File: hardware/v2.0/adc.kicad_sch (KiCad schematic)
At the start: 1 part, among them U1 ECP5U-25F-CABGA256

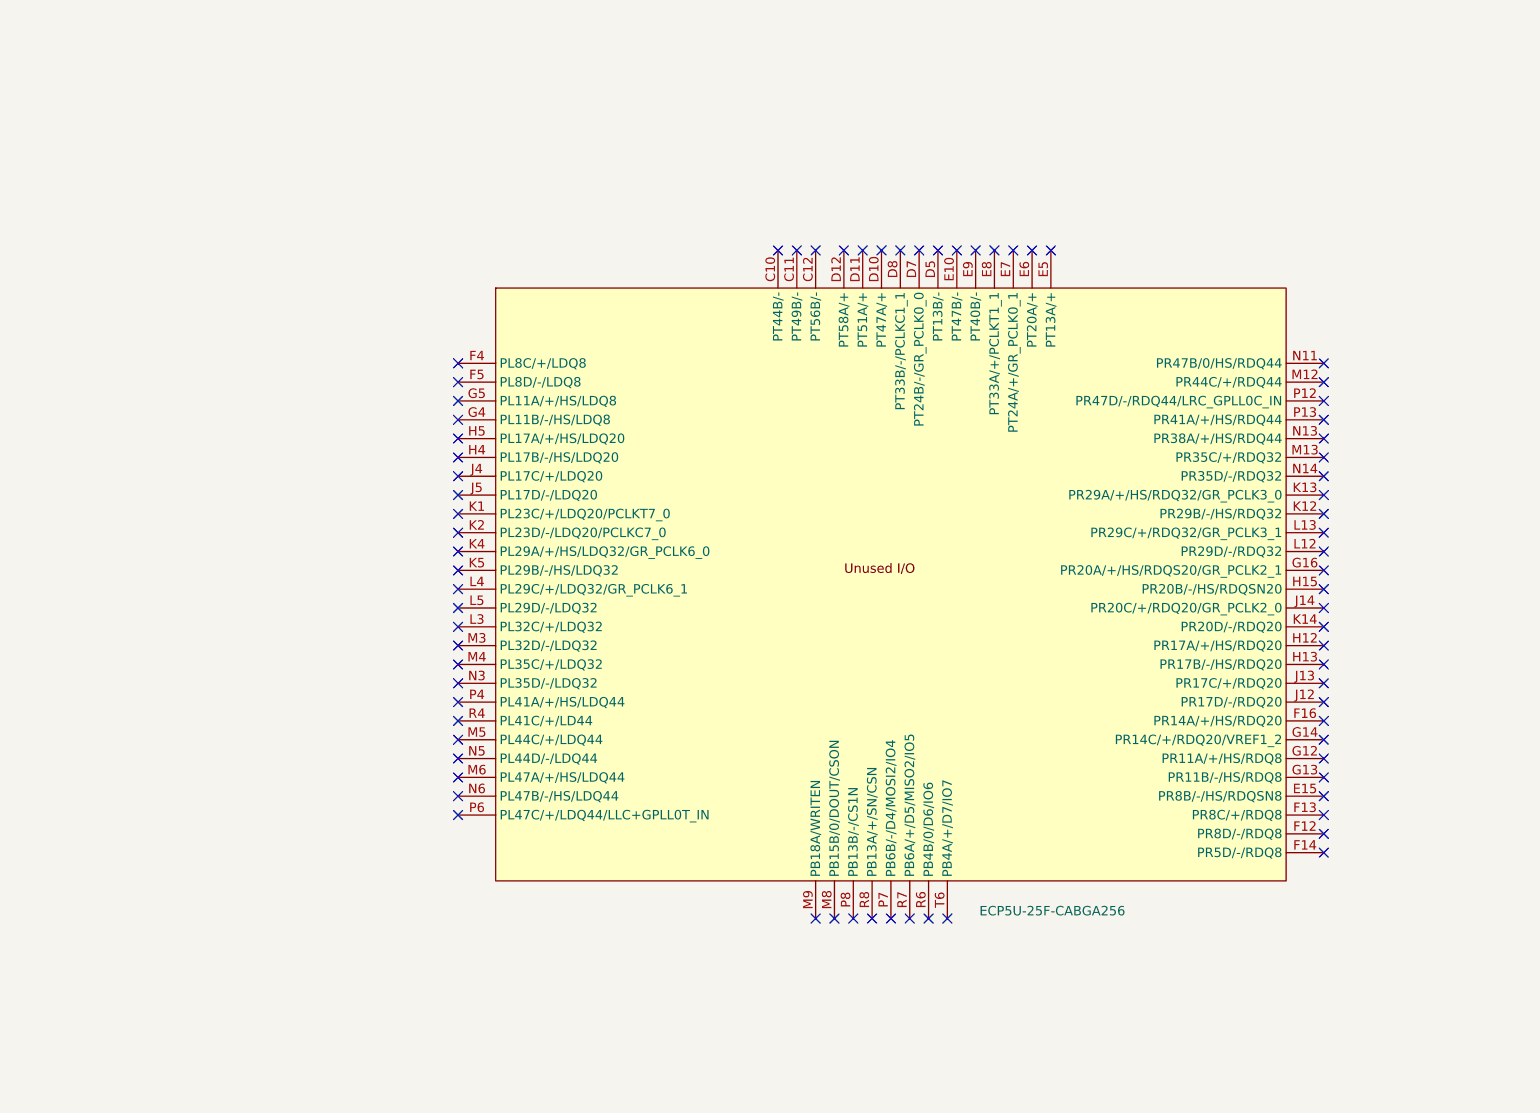
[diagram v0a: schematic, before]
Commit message: Initial plan for adding an external ADC
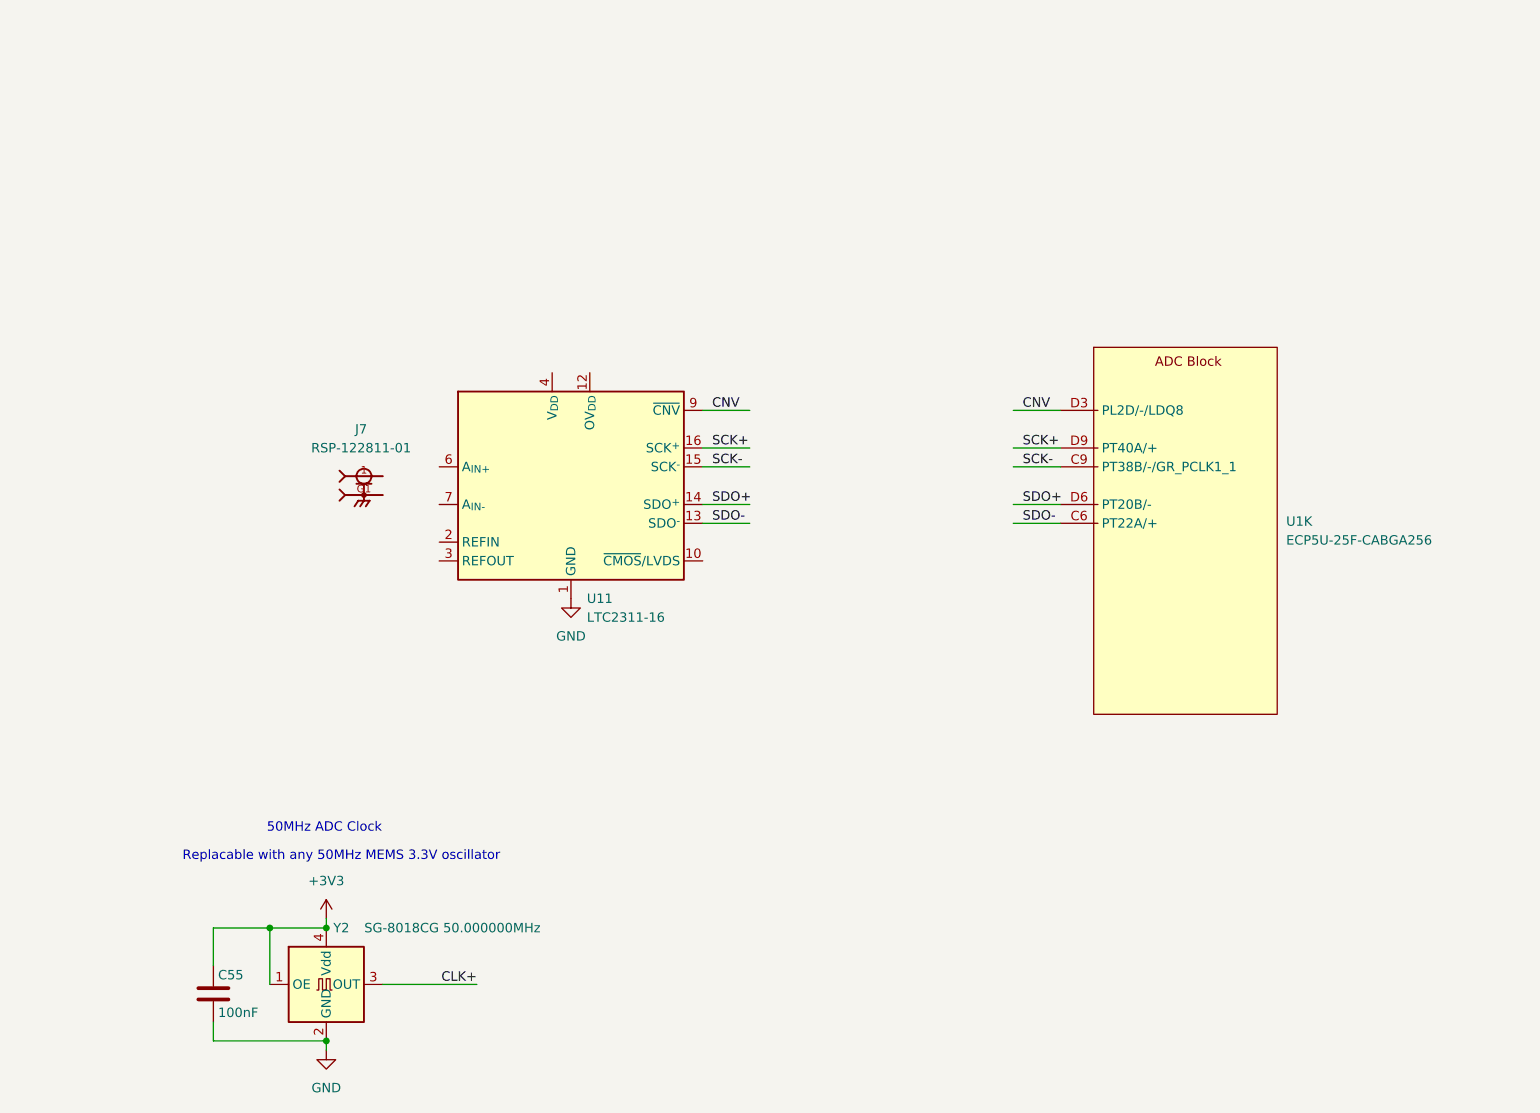
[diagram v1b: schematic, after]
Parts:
- removed U1: ECP5U-25F-CABGA256, Package_BGA:BGA-256_14.0x14.0mm_Layout16x16_P0.8mm_Ball0.45mm_Pad0.32mm_NSMD, symbol icepi-lib:LFE5U-25F-6BG256x
- added C55: 100nF, Capacitor_SMD:C_0402_1005Metric, symbol Device:C
- added J7: RSP-122811-01, RSP-122811-01:SAMTEC_RSP-122811-01, symbol RSP-122811-01:RSP-122811-01
- added U1: ECP5U-25F-CABGA256, Package_BGA:BGA-256_14.0x14.0mm_Layout16x16_P0.8mm_Ball0.45mm_Pad0.32mm_NSMD, symbol icepi-lib:LFE5U-25F-6BG256x
- added U11: LTC2311-16, Package_SO:MSOP-16-1EP_3x4.039mm_P0.5mm_EP1.651x2.845mm, symbol Analog_ADC:LTC2311-16
- added Y2: SG-8018CG 50.000000MHz, Oscillator:Oscillator_SMD_SiT_PQFN-4Pin_2.5x2.0mm, symbol Oscillator:SiT8008xx-1x-xxE
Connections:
- new net: J7.G1, J7.G2
- new net +3V3: C55.1, Y2.1 (OE), Y2.4 (Vdd)
- new net CLK+: Y2.3 (OUT)
- new net CNV: U1.D3 (PL2D/-/LDQ8), U11.9 (~{CNV})
- new net GND: C55.2, U11.1 (GND), U11.11 (GND), U11.17 (GND), U11.5 (GND), U11.8 (GND), Y2.2 (GND)
- new net SCK+: U1.D9 (PT40A/+), U11.16 (SCK^{+})
- new net SCK-: U1.C9 (PT38B/-/GR_PCLK1_1), U11.15 (SCK^{-})
- new net SDO+: U1.D6 (PT20B/-), U11.14 (SDO^{+})
- new net SDO-: U1.C6 (PT22A/+), U11.13 (SDO^{-})
- no-connect marks 75 -> 0
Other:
- note added: "50MHz ADC Clock"
- note added: "Replacable with any 50MHz MEMS 3.3V oscillator"
- title: Icepi Zero -> (none)

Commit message: Minor changes
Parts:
- added R51, R52: 100, Resistor_SMD:R_0402_1005Metric, symbol Device:R
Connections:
- net SCK+: now also R52.1
- net SCK-: now also R52.2
- net SDO+: now also R51.2
- net SDO-: now also R51.1
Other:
- moved on the sheet: U1K

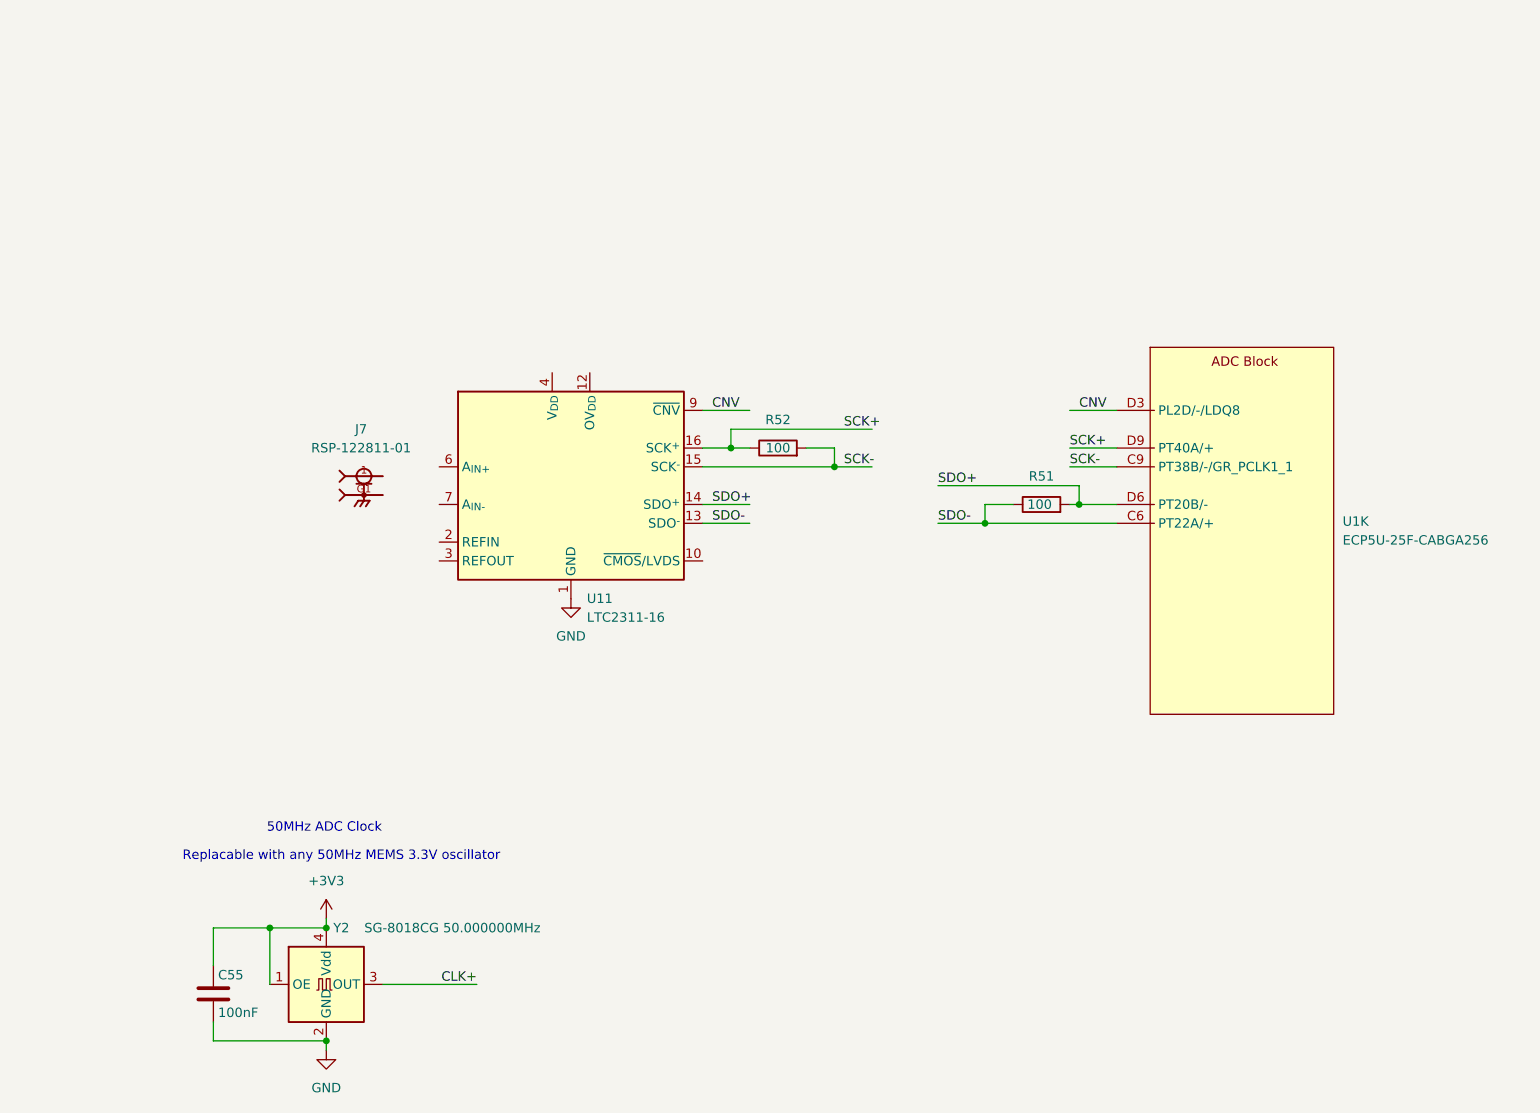
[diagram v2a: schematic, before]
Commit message: LDOs dividers update
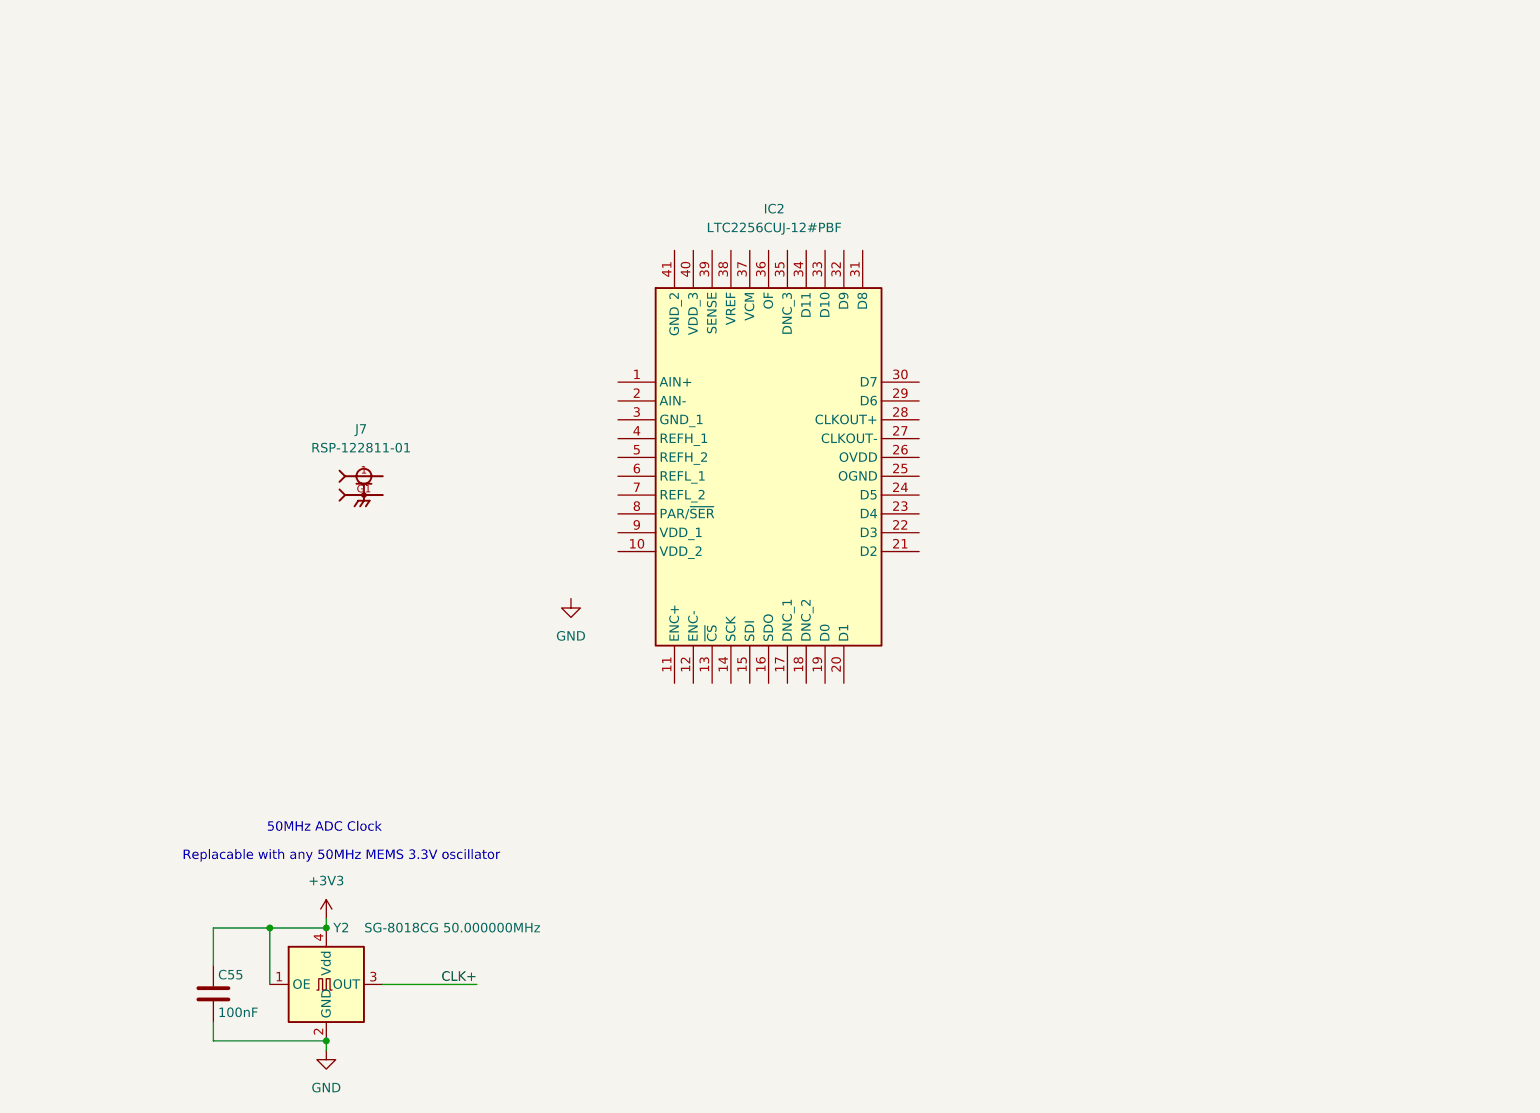
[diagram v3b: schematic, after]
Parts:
- removed R51, R52: 100, Resistor_SMD:R_0402_1005Metric, symbol Device:R
- removed U1: ECP5U-25F-CABGA256, Package_BGA:BGA-256_14.0x14.0mm_Layout16x16_P0.8mm_Ball0.45mm_Pad0.32mm_NSMD, symbol icepi-lib:LFE5U-25F-6BG256x
- removed U11: LTC2311-16, Package_SO:MSOP-16-1EP_3x4.039mm_P0.5mm_EP1.651x2.845mm, symbol Analog_ADC:LTC2311-16
- added IC2: LTC2256CUJ-12#PBF, QFN50P600X600X80-41N-D, symbol LTC2256CUJ-12#PBF:LTC2256CUJ-12#PBF

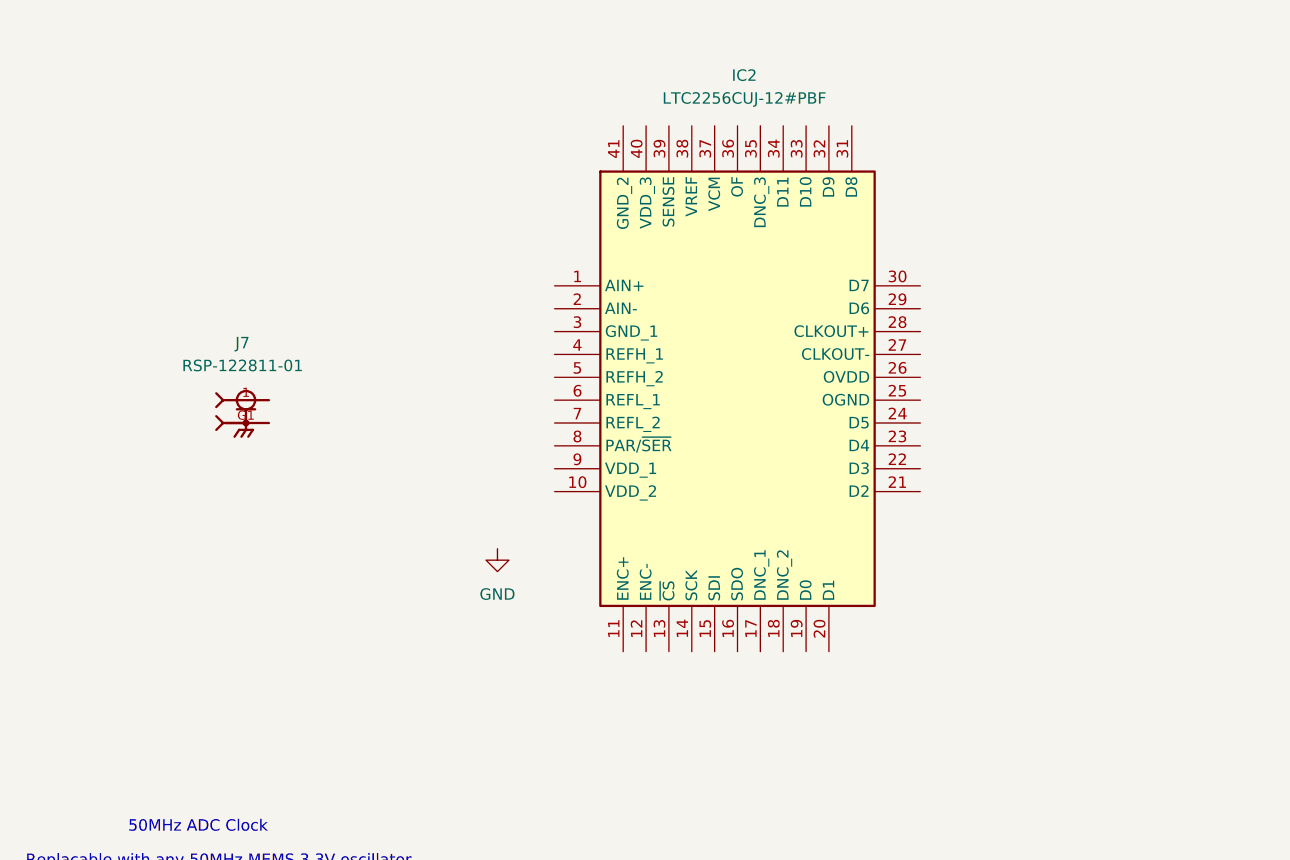
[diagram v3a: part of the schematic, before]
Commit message: ADC 6 diff lines
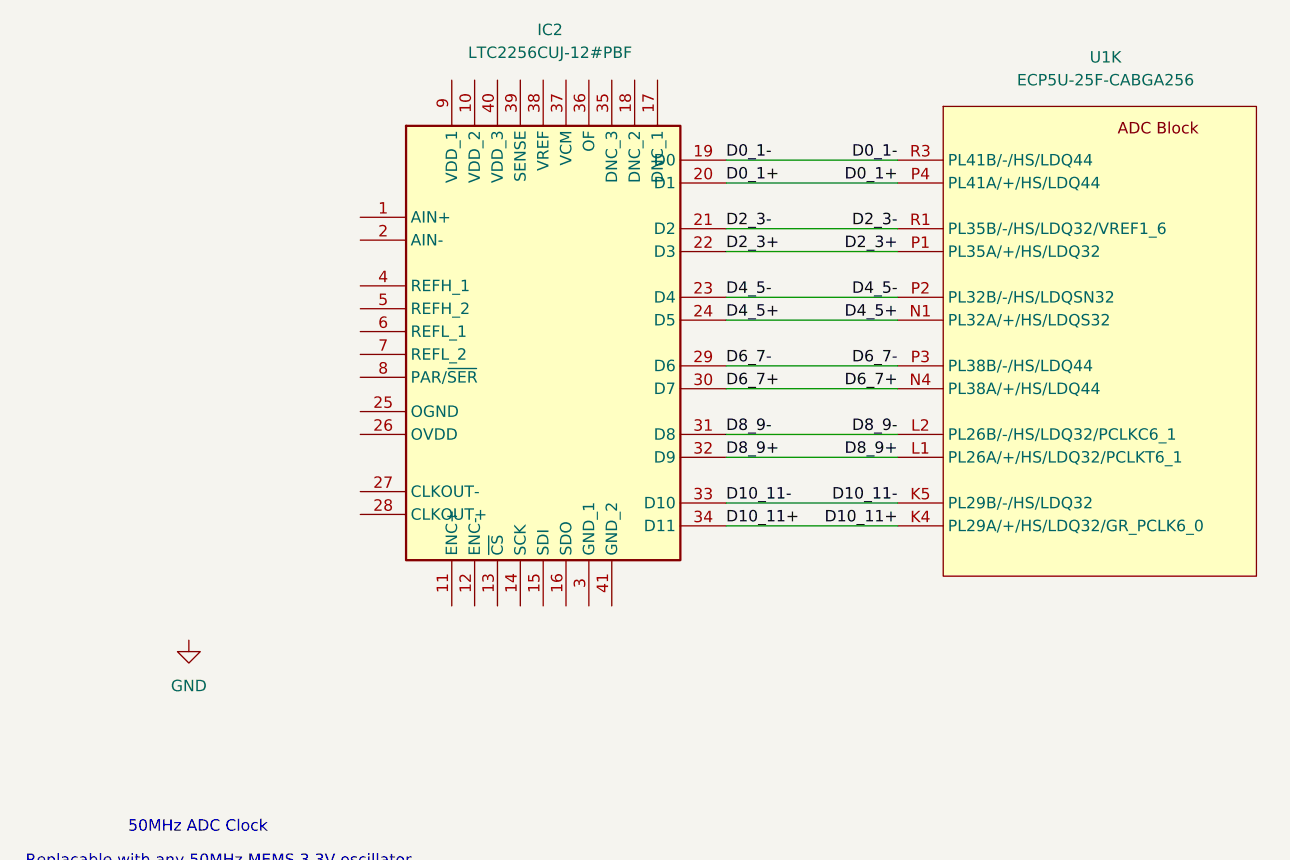
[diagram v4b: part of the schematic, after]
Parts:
- removed J7: RSP-122811-01, RSP-122811-01:SAMTEC_RSP-122811-01, symbol RSP-122811-01:RSP-122811-01
- added U1: ECP5U-25F-CABGA256, Package_BGA:BGA-256_14.0x14.0mm_Layout16x16_P0.8mm_Ball0.45mm_Pad0.32mm_NSMD, symbol icepi-lib:LFE5U-25F-6BG256x
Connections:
- net D0_1-: now reaches IC2.19 (D0)
- net D0_1-: now also U1.R3 (PL41B/-/HS/LDQ44)
- net D0_1+: now reaches IC2.20 (D1)
- net D0_1+: now also U1.P4 (PL41A/+/HS/LDQ44)
- net D2_3-: now reaches IC2.21 (D2)
- net D2_3-: now also U1.R1 (PL35B/-/HS/LDQ32/VREF1_6)
- net D2_3+: now reaches IC2.22 (D3)
- net D2_3+: now also U1.P1 (PL35A/+/HS/LDQ32)
- net D4_5-: now reaches IC2.23 (D4)
- net D4_5-: now also U1.P2 (PL32B/-/HS/LDQSN32)
- net D4_5+: now reaches IC2.24 (D5)
- net D4_5+: now also U1.N1 (PL32A/+/HS/LDQS32)
- net D6_7-: now reaches IC2.29 (D6)
- net D6_7-: now also U1.P3 (PL38B/-/HS/LDQ44)
- net D6_7+: now reaches IC2.30 (D7)
- net D6_7+: now also U1.N4 (PL38A/+/HS/LDQ44)
- net D8_9-: now reaches IC2.31 (D8)
- net D8_9-: now also U1.L2 (PL26B/-/HS/LDQ32/PCLKC6_1)
- net D8_9+: now reaches IC2.32 (D9)
- net D8_9+: now also U1.L1 (PL26A/+/HS/LDQ32/PCLKT6_1)
- net D10_11-: now reaches IC2.33 (D10)
- net D10_11-: now also U1.K5 (PL29B/-/HS/LDQ32)
- net D10_11+: now reaches IC2.34 (D11)
- net D10_11+: now also U1.K4 (PL29A/+/HS/LDQ32/GR_PCLK6_0)
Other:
- moved on the sheet: IC2
